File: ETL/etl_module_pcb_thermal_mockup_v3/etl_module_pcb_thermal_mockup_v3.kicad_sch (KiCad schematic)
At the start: 13 parts, among them J1 WP7B-S050VA1-R8000, J2 WP7B-S050VA1-R8000, J3 Conn_02x02_Odd_Even, J4 Conn_02x08_Counter_Clockwise, J5 Conn_02x08_Counter_Clockwise, J6 Conn_02x08_Counter_Clockwise, J7 Conn_02x08_Counter_Clockwise, U1 ETROC_dummy_thermal_sensors, U2 ETROC_dummy_thermal_sensors, U3 ETROC_dummy_thermal_sensors, U4 ETROC_dummy_thermal_sensors

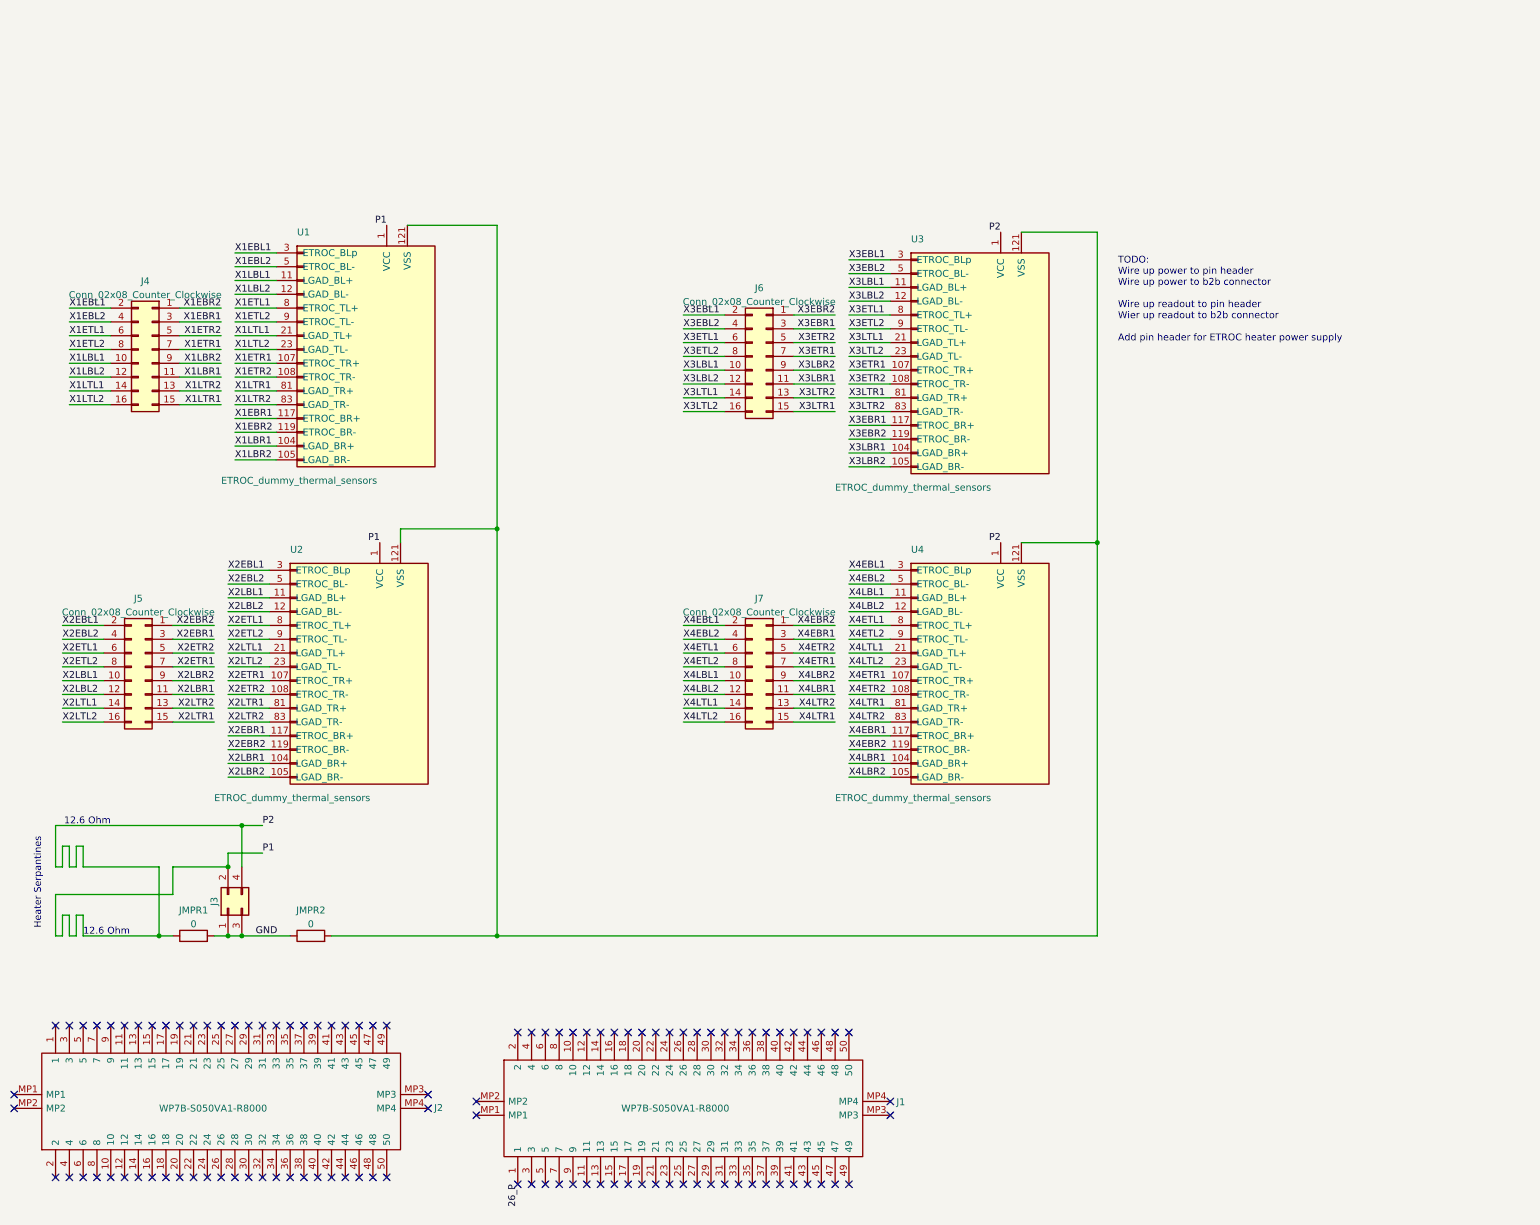
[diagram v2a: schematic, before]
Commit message: Reworking of etl_module_pcb_thermal_mockup_v3 to embed ADCs for easier monitoring
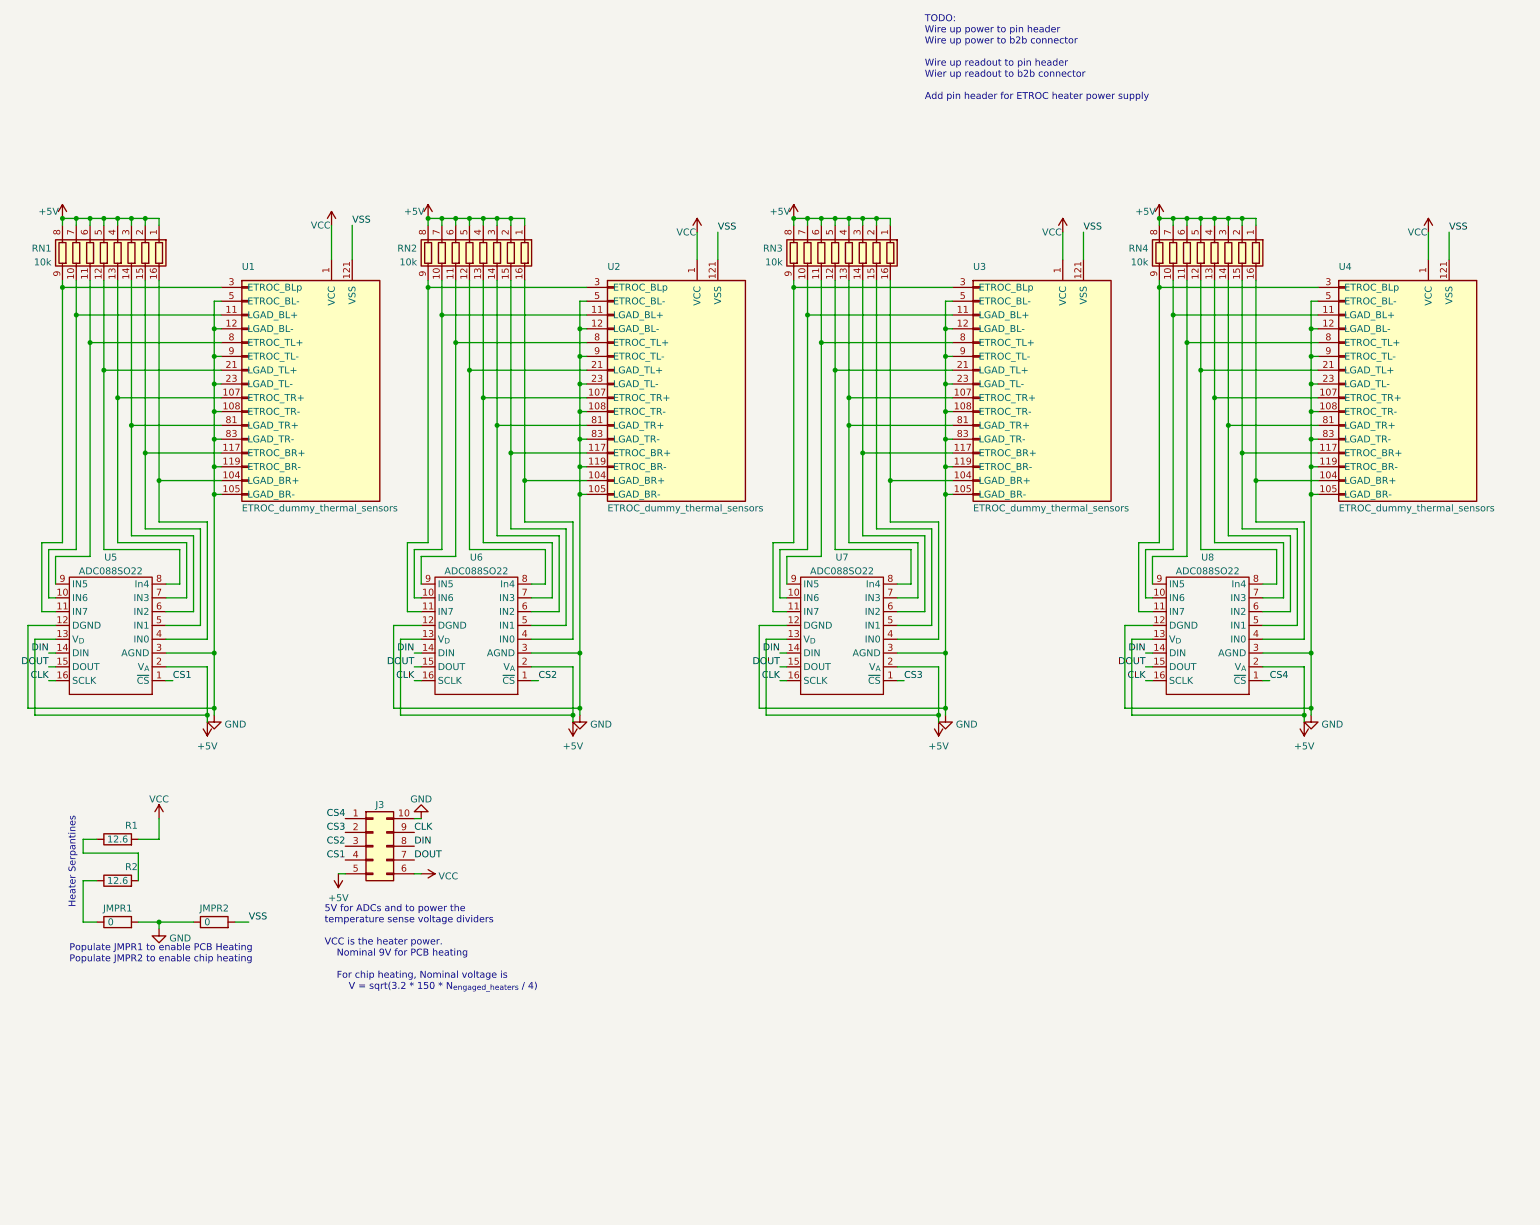
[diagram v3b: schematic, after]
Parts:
- removed J1, J2: WP7B-S050VA1-R8000, SamacSys_Parts:WP7BS050VA1R8000, symbol SamacSys_Parts:WP7B-S050VA1-R8000
- removed J3: Conn_02x02_Odd_Even, Connector_PinHeader_2.54mm:PinHeader_2x02_P2.54mm_Vertical_SMD, symbol Connector_Generic:Conn_02x02_Odd_Even
- removed J4, J5, J6, J7: Conn_02x08_Counter_Clockwise, Connector_PinHeader_1.27mm:PinHeader_2x08_P1.27mm_Vertical_SMD, symbol Connector_Generic:Conn_02x08_Odd_Even
- added J3: Conn_02x05_Counter_Clockwise, Connector_PinHeader_2.54mm:PinHeader_2x05_P2.54mm_Vertical_SMD, symbol Connector_Generic:Conn_02x05_Counter_Clockwise
- added R1, R2: 12.6, unl_silab:ETROC_Heater_Serpantine, symbol Device:R
- added RN1, RN2, RN3, RN4: 10k, Resistor_SMD:R_Array_Convex_8x0602, symbol Device:R_Pack08
- added U5, U6, U7, U8: ADC088SO22, Package_SO:TSSOP-16_4.4x5mm_P0.65mm, symbol unl_silab:ADC088SO22
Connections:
- net X1EBL2 is gone; now on net GND: U1.5 (ETROC_BL-)
- net X1EBR2 is gone; now on net GND: U1.119 (ETROC_BR-)
- net X1ETL2 is gone; now on net GND: U1.9 (ETROC_TL-)
- net X1ETR2 is gone; now on net GND: U1.108 (ETROC_TR-)
- net X1LBL2 is gone; now on net GND: U1.12 (LGAD_BL-)
- net X1LBR2 is gone; now on net GND: U1.105 (LGAD_BR-)
- net X1LTL2 is gone; now on net GND: U1.23 (LGAD_TL-)
- net X1LTR2 is gone; now on net GND: U1.83 (LGAD_TR-)
- net X2EBL2 is gone; now on net GND: U2.5 (ETROC_BL-)
- net X2EBR2 is gone; now on net GND: U2.119 (ETROC_BR-)
- net X2ETL2 is gone; now on net GND: U2.9 (ETROC_TL-)
- net X2ETR2 is gone; now on net GND: U2.108 (ETROC_TR-)
- net X2LBL2 is gone; now on net GND: U2.12 (LGAD_BL-)
- net X2LBR2 is gone; now on net GND: U2.105 (LGAD_BR-)
- net X2LTL2 is gone; now on net GND: U2.23 (LGAD_TL-)
- net X2LTR2 is gone; now on net GND: U2.83 (LGAD_TR-)
- net X3EBL2 is gone; now on net GND: U3.5 (ETROC_BL-)
- net X3EBR2 is gone; now on net GND: U3.119 (ETROC_BR-)
- net X3ETL2 is gone; now on net GND: U3.9 (ETROC_TL-)
- net X3ETR2 is gone; now on net GND: U3.108 (ETROC_TR-)
- net X3LBL2 is gone; now on net GND: U3.12 (LGAD_BL-)
- net X3LBR2 is gone; now on net GND: U3.105 (LGAD_BR-)
- net X3LTL2 is gone; now on net GND: U3.23 (LGAD_TL-)
- net X3LTR1 is gone; now on an unnamed net: U3.81 (LGAD_TR+)
- net X3LTR2 is gone; now on net GND: U3.83 (LGAD_TR-)
- net X4EBL2 is gone; now on net GND: U4.5 (ETROC_BL-)
- net X4EBR2 is gone; now on net GND: U4.119 (ETROC_BR-)
- net X4ETL2 is gone; now on net GND: U4.9 (ETROC_TL-)
- net X4ETR2 is gone; now on net GND: U4.108 (ETROC_TR-)
- net X4LBL2 is gone; now on net GND: U4.12 (LGAD_BL-)
- net X4LBR2 is gone; now on net GND: U4.105 (LGAD_BR-)
- net X4LTL2 is gone; now on net GND: U4.23 (LGAD_TL-)
- net X4LTR2 is gone; now on net GND: U4.83 (LGAD_TR-)
- net GND: now also J3.10 (Pin_10), U5.12 (DGND), U5.3 (AGND), U6.12 (DGND), U6.3 (AGND), U7.12 (DGND), U7.3 (AGND), U8.12 (DGND), U8.3 (AGND)
- net VSS: now reaches JMPR2.2, U1.121 (VSS), U2.121 (VSS), U3.121 (VSS), U4.121 (VSS)
- net P1 renamed VCC
- net VCC: now also J3.6 (Pin_6), R1.2; no longer JMPR1.1
- net X1EBL1: no longer names the net of U1.3 (ETROC_BLp)
- net X1EBL1: now also RN1.9 (R8.2), U5.11 (IN7)
- net X1EBR1: no longer names the net of U1.117 (ETROC_BR+)
- net X1EBR1: now also RN1.15 (R2.2), U5.5 (IN1)
- net X1ETL1: no longer names the net of U1.8 (ETROC_TL+)
- net X1ETL1: now also RN1.11 (R6.2), U5.9 (IN5)
- net X1ETR1: no longer names the net of U1.107 (ETROC_TR+)
- net X1ETR1: now also RN1.13 (R4.2), U5.7 (IN3)
- net X1LBL1: no longer names the net of U1.11 (LGAD_BL+)
- net X1LBL1: now also RN1.10 (R7.2), U5.10 (IN6)
- net X1LBR1: no longer names the net of U1.104 (LGAD_BR+)
- net X1LBR1: now also RN1.16 (R1.2), U5.4 (IN0)
- net X1LTL1: no longer names the net of U1.21 (LGAD_TL+)
- net X1LTL1: now also RN1.12 (R5.2), U5.8 (In4)
- net X1LTR1: no longer names the net of U1.81 (LGAD_TR+)
- net X1LTR1: now also RN1.14 (R3.2), U5.6 (IN2)
- net X2EBL1: no longer names the net of U2.3 (ETROC_BLp)
- net X2EBL1: now also RN2.9 (R8.2), U6.11 (IN7)
- net X2EBR1: no longer names the net of U2.117 (ETROC_BR+)
- net X2EBR1: now also RN2.15 (R2.2), U6.5 (IN1)
- net X2ETL1: no longer names the net of U2.8 (ETROC_TL+)
- net X2ETL1: now also RN2.11 (R6.2), U6.9 (IN5)
- net X2ETR1: no longer names the net of U2.107 (ETROC_TR+)
- net X2ETR1: now also RN2.13 (R4.2), U6.7 (IN3)
- net X2LBL1: no longer names the net of U2.11 (LGAD_BL+)
- net X2LBL1: now also RN2.10 (R7.2), U6.10 (IN6)
- net X2LBR1: no longer names the net of U2.104 (LGAD_BR+)
- net X2LBR1: now also RN2.16 (R1.2), U6.4 (IN0)
- net X2LTL1: no longer names the net of U2.21 (LGAD_TL+)
- net X2LTL1: now also RN2.12 (R5.2), U6.8 (In4)
- net X2LTR1: no longer names the net of U2.81 (LGAD_TR+)
- net X2LTR1: now also RN2.14 (R3.2), U6.6 (IN2)
- net X3EBL1: no longer names the net of U3.3 (ETROC_BLp)
- net X3EBL1: now also RN3.9 (R8.2), U7.11 (IN7)
- net X3EBR1: no longer names the net of U3.117 (ETROC_BR+)
- net X3EBR1: now also RN3.14 (R3.2), U7.6 (IN2)
- net X3ETL1: no longer names the net of U3.8 (ETROC_TL+)
- net X3ETL1: now also RN3.11 (R6.2), U7.9 (IN5)
- net X3ETR1: no longer names the net of U3.107 (ETROC_TR+)
- net X3ETR1: now also RN3.13 (R4.2), U7.7 (IN3)
- net X3LBL1: no longer names the net of U3.11 (LGAD_BL+)
- net X3LBL1: now also RN3.10 (R7.2), U7.10 (IN6)
- net X3LBR1: no longer names the net of U3.104 (LGAD_BR+)
- net X3LBR1: now also RN3.16 (R1.2), U7.4 (IN0)
- net X3LTL1: no longer names the net of U3.21 (LGAD_TL+)
- net X3LTL1: now also RN3.12 (R5.2), U7.8 (In4)
- net X4EBL1: no longer names the net of U4.3 (ETROC_BLp)
- net X4EBL1: now also RN4.9 (R8.2), U8.11 (IN7)
- net X4EBR1: no longer names the net of U4.117 (ETROC_BR+)
- net X4EBR1: now also RN4.15 (R2.2), U8.5 (IN1)
- net X4ETL1: no longer names the net of U4.8 (ETROC_TL+)
- net X4ETL1: now also RN4.11 (R6.2), U8.9 (IN5)
- net X4ETR1: no longer names the net of U4.107 (ETROC_TR+)
- net X4ETR1: now also RN4.13 (R4.2), U8.7 (IN3)
- net X4LBL1: no longer names the net of U4.11 (LGAD_BL+)
- net X4LBL1: now also RN4.10 (R7.2), U8.10 (IN6)
- net X4LBR1: no longer names the net of U4.104 (LGAD_BR+)
- net X4LBR1: now also RN4.16 (R1.2), U8.4 (IN0)
- net X4LTL1: no longer names the net of U4.21 (LGAD_TL+)
- net X4LTL1: now also RN4.12 (R5.2), U8.8 (In4)
- net X4LTR1: no longer names the net of U4.81 (LGAD_TR+)
- net X4LTR1: now also RN4.14 (R3.2), U8.6 (IN2)
- new net: R1.1, R2.2
- new net: RN3.15 (R2.2), U7.5 (IN1)
- new net: JMPR1.1, R2.1
- new net +5V: J3.5 (Pin_5), RN1.1 (R1.1), RN1.2 (R2.1), RN1.3 (R3.1), RN1.4 (R4.1), RN1.5 (R5.1), RN1.6 (R6.1), RN1.7 (R7.1), RN1.8 (R8.1), RN2.1 (R1.1), RN2.2 (R2.1), RN2.3 (R3.1), RN2.4 (R4.1), RN2.5 (R5.1), RN2.6 (R6.1), RN2.7 (R7.1), RN2.8 (R8.1), RN3.1 (R1.1), RN3.2 (R2.1), RN3.3 (R3.1), RN3.4 (R4.1), RN3.5 (R5.1), RN3.6 (R6.1), RN3.7 (R7.1), RN3.8 (R8.1), RN4.1 (R1.1), RN4.2 (R2.1), RN4.3 (R3.1), RN4.4 (R4.1), RN4.5 (R5.1), RN4.6 (R6.1), RN4.7 (R7.1), RN4.8 (R8.1), U5.13 (V_{D}), U5.2 (V_{A}), U6.13 (V_{D}), U6.2 (V_{A}), U7.13 (V_{D}), U7.2 (V_{A}), U8.13 (V_{D}), U8.2 (V_{A})
- new net CLK: J3.9 (Pin_9), U5.16 (SCLK), U6.16 (SCLK), U7.16 (SCLK), U8.16 (SCLK)
- new net CS1: J3.4 (Pin_4), U5.1 (~{CS})
- new net CS2: J3.3 (Pin_3), U6.1 (~{CS})
- new net CS3: J3.2 (Pin_2), U7.1 (~{CS})
- new net CS4: J3.1 (Pin_1), U8.1 (~{CS})
- new net DIN: J3.8 (Pin_8), U5.14 (DIN), U6.14 (DIN), U7.14 (DIN), U8.14 (DIN)
- new net DOUT: J3.7 (Pin_7), U5.15 (DOUT), U6.15 (DOUT), U7.15 (DOUT), U8.15 (DOUT)
- no-connect marks 108 -> 0
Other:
- note added: "5V for ADCs and to power the temperature sense voltage dividers VCC is the heater power. Nominal 9V for PCB heating For chip heating, Nominal voltage is V = sqrt(3.2 * 150 * N_{engaged_heaters} / 4)"
- note added: "Populate JMPR1 to enable PCB Heating Populate JMPR2 to enable chip heating"
- note removed: "12.6 Ohm"
- moved on the sheet: JMPR1, JMPR2, U1, U2, U3, U4

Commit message: Finishes redesigned draft of etl_module_pcb_thermal_mockup_v3
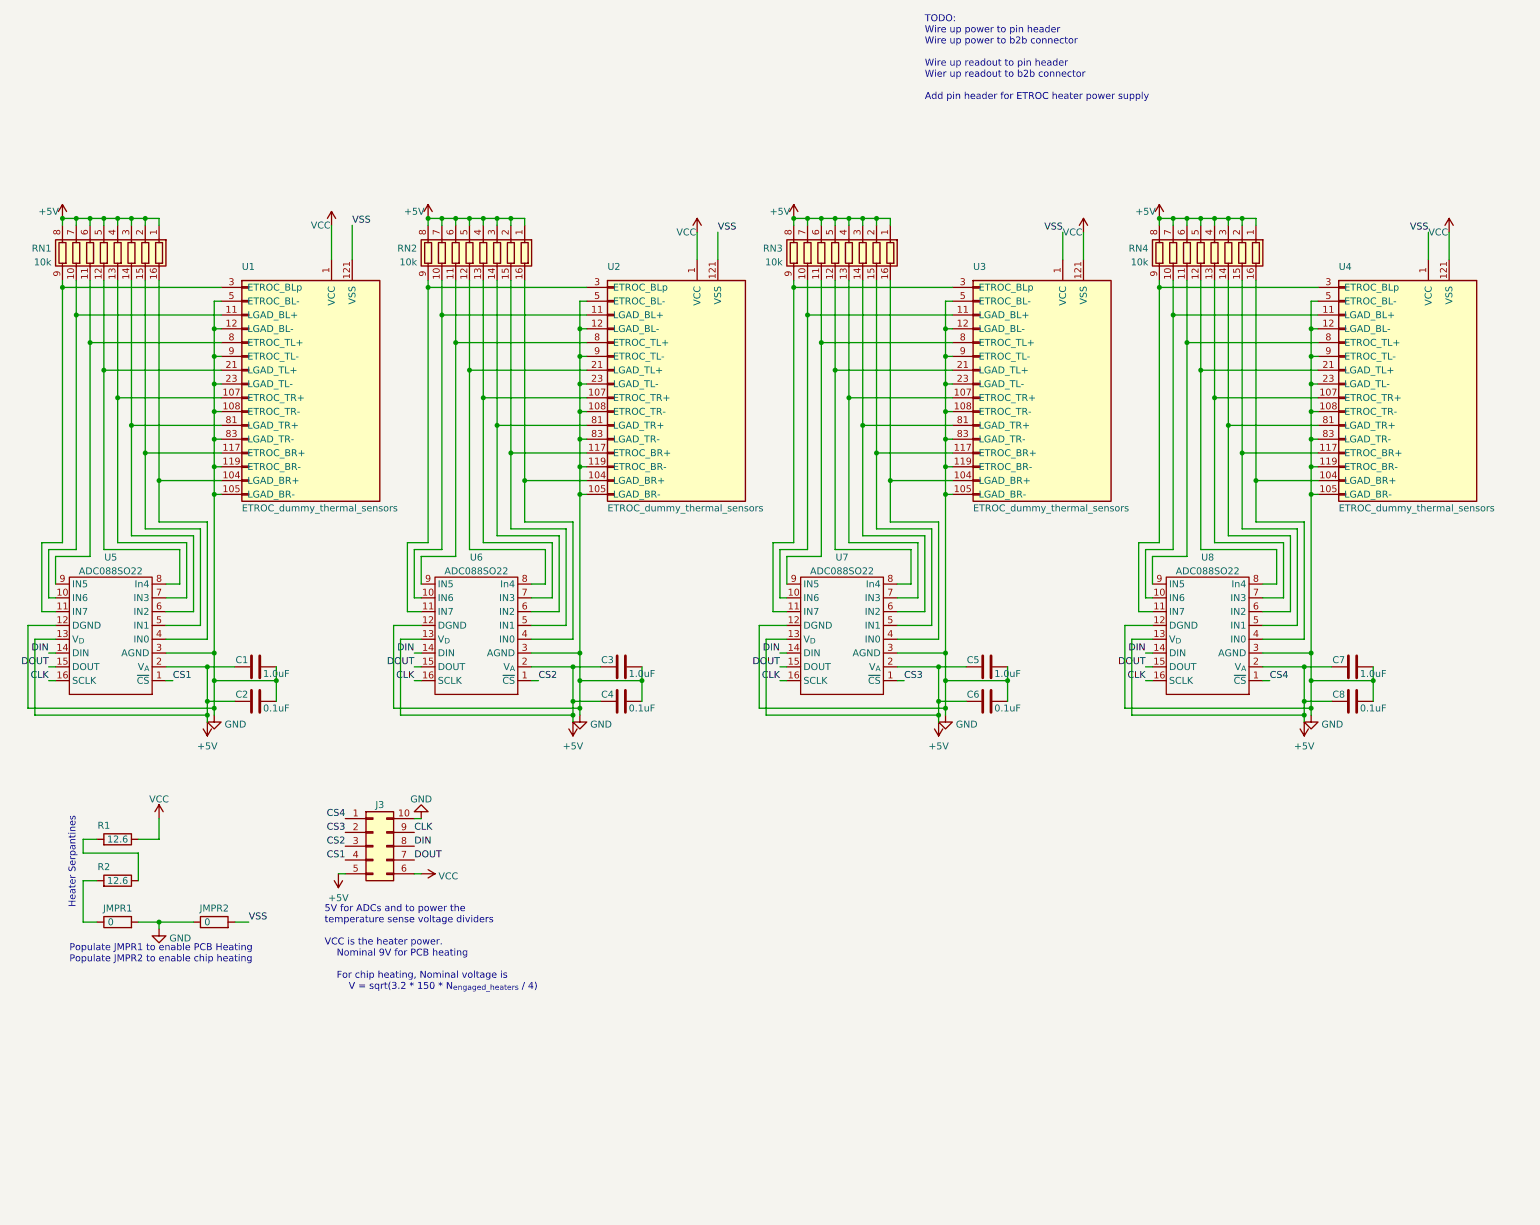
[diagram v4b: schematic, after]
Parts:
- added C1, C3, C5, C7: 1.0uF, Capacitor_SMD:C_0201_0603Metric_Pad0.64x0.40mm_HandSolder, symbol Device:C
- added C2, C4, C6, C8: 0.1uF, Capacitor_SMD:C_0201_0603Metric_Pad0.64x0.40mm_HandSolder, symbol Device:C
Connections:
- net +5V: now also C1.1, C2.1, C3.1, C4.1, C5.1, C6.1, C7.1, C8.1
- net GND: now also C1.2, C2.2, C3.2, C4.2, C5.2, C6.2, C7.2, C8.2
- net VCC: now also R1.1, U3.121 (VSS), U4.121 (VSS); no longer R1.2, U3.1 (VCC), U4.1 (VCC)
- net VSS: now also U3.1 (VCC), U4.1 (VCC); no longer U3.121 (VSS), U4.121 (VSS)
- net at R2.2: now also JMPR1.1; no longer R1.1
- net at RN3.13 (R4.2), U3.107 (ETROC_TR+), U7.7 (IN3): no longer U3.81 (LGAD_TR+)
- net at RN3.14 (R3.2), U7.6 (IN2): now also U3.81 (LGAD_TR+); no longer U3.117 (ETROC_BR+)
- net at RN3.15 (R2.2), U7.5 (IN1): now also U3.117 (ETROC_BR+)
- net at R2.1: now also R1.2; no longer JMPR1.1
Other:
- moved on the sheet: R1, R2
